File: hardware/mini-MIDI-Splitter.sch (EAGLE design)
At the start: 40 parts, among them IC1 6N138, IC2 4050D, IC3 REG1117, X1 DIN5PIN, X2 DIN5PIN, X3 DIN5PIN, X4 DIN5PIN, X5 DIN5PIN, X6 DIN5PIN

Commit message: updates
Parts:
- C3: device rcl:CPOL-EUE2-4 -> rcl:C-EUC0805
- C5: device rcl:C-EUC0805 -> rcl:CPOL-EUE2-4
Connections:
- net GND: now also C3.2, C5.-, R3.1; no longer C3.-, C5.2, R2.1
- net N$1: now also R5.2; no longer R4.2
- net N$11: now also R7.1; no longer R6.1
- net N$12: now also R5.1; no longer R4.1
- net N$14: now also R4.1; no longer R5.1
- net N$15: now also R6.1; no longer R7.1
- net N$16: now also R8.1; no longer R9.1
- net N$18: now also R12.1; no longer R18.1
- net N$19: now also R17.1; no longer R16.1
- net N$2: now also R7.2; no longer R6.2
- net N$20: now also R2.1; no longer R3.1
- net N$21: now also R2.2; no longer R3.2
- net N$22: now also R3.2; no longer R2.2
- net N$3: now also R9.2; no longer R8.2
- net N$5: now also R18.2; no longer R12.2
- net N$6: now also R16.2; no longer R17.2
- net N$7: now also R16.1; no longer R17.1
- net N$8: now also R9.1; no longer R8.1
- net N$9: now also R18.1; no longer R12.1
- net VCC: now also C1.1, C5.+, R12.2, R17.2, R4.2, R6.2, R8.2; no longer C4.+, C5.1, R16.2, R18.2, R5.2, R7.2, R9.2
- net VIN: now also C3.1, C4.+; no longer C1.1, C3.+
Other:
- moved on the sheet: C1, C4, R12, R16, R17, R18, R2, R3, R4, R5, R6, R7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

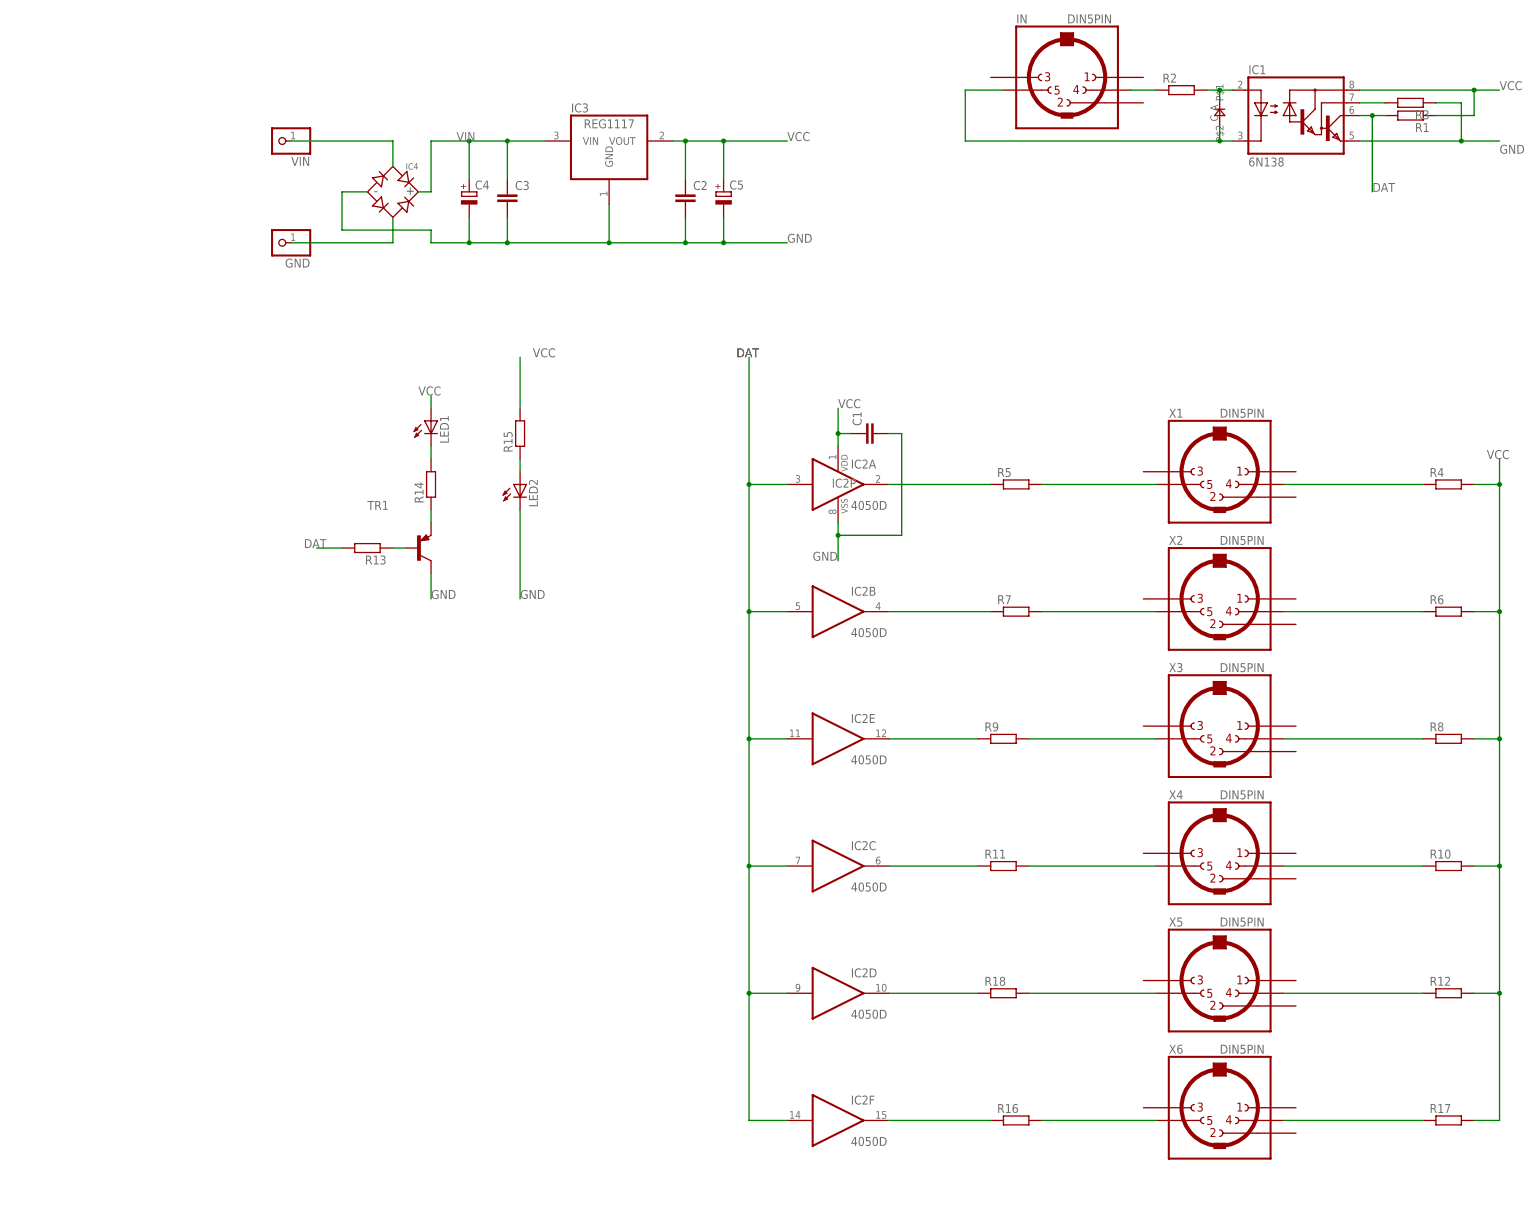
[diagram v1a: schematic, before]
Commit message: add component values
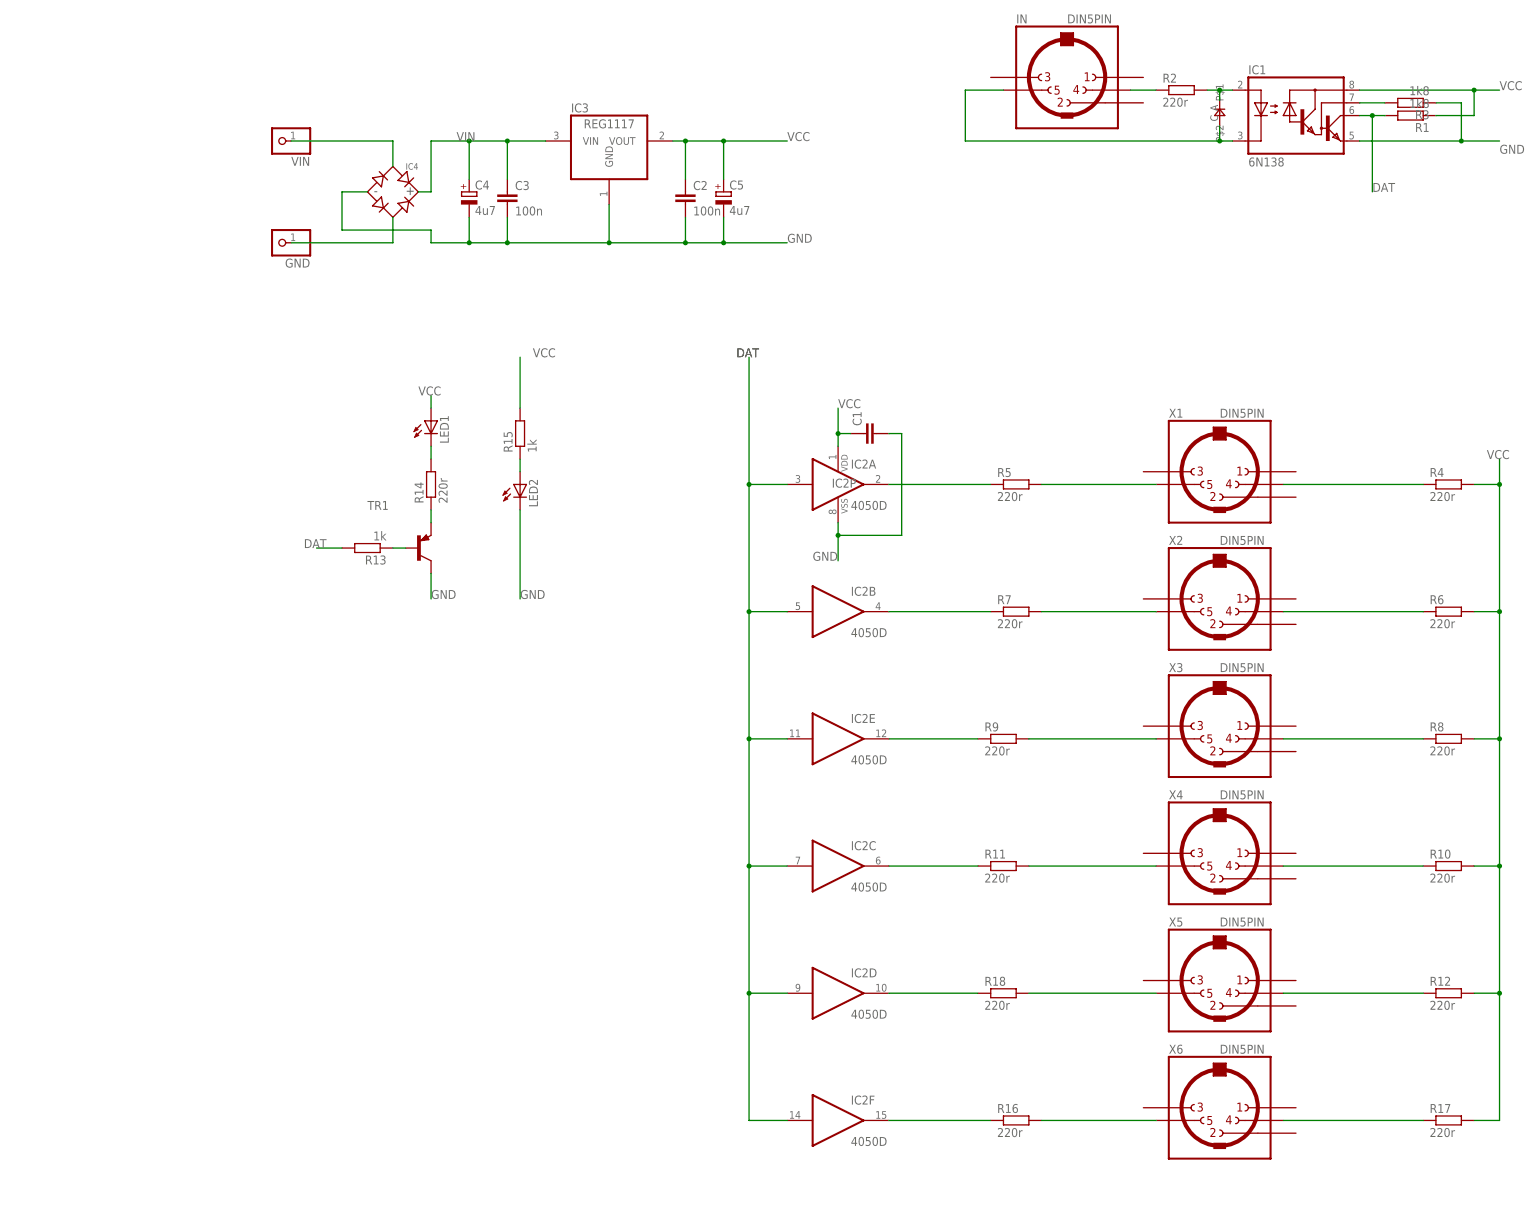
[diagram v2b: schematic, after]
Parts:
- C2, C3: value (none) -> 100n
- C4, C5: value (none) -> 4u7
- R1, R3: value (none) -> 1k8
- R10, R11, R12, R14, R16, R17, R18, R2, R4, R5, R6, R7, R8, R9: value (none) -> 220r
- R13, R15: value (none) -> 1k
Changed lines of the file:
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@@
 <part name="IN" library="jason_eagle6" deviceset="DIN5PIN" device=""/>
 <part name="IC2" library="40xx" deviceset="4050" device="D"/>
-<part name="R5" library="rcl" deviceset="R-EU_" device="R0805"/>
-<part name="R7" library="rcl" deviceset="R-EU_" device="R0805"/>
-<part name="R11" library="rcl" deviceset="R-EU_" device="R0805"/>
-<part name="R18" library="rcl" deviceset="R-EU_" device="R0805"/>
-<part name="R9" library="rcl" deviceset="R-EU_" device="R0805"/>
-<part name="R16" library="rcl" deviceset="R-EU_" device="R0805"/>
-<part name="R4" library="rcl" deviceset="R-EU_" device="R0805"/>
-<part name="R6" library="rcl" deviceset="R-EU_" device="R0805"/>
-<part name="R8" library="rcl" deviceset="R-EU_" device="R0805"/>
-<part name="R10" library="rcl" deviceset="R-EU_" device="R0805"/>
-<part name="R12" library="rcl" deviceset="R-EU_" device="R0805"/>
-<part name="R17" library="rcl" deviceset="R-EU_" device="R0805"/>
+<part name="R5" library="rcl" deviceset="R-EU_" device="R0805" value="220r"/>
+<part name="R7" library="rcl" deviceset="R-EU_" device="R0805" value="220r"/>
+<part name="R11" library="rcl" deviceset="R-EU_" device="R0805" value="220r"/>
+<part name="R18" library="rcl" deviceset="R-EU_" device="R0805" value="220r"/>
+<part name="R9" library="rcl" deviceset="R-EU_" device="R0805" value="220r"/>
+<part name="R16" library="rcl" deviceset="R-EU_" device="R0805" value="220r"/>
+<part name="R4" library="rcl" deviceset="R-EU_" device="R0805" value="220r"/>
+<part name="R6" library="rcl" deviceset="R-EU_" device="R0805" value="220r"/>
+<part name="R8" library="rcl" deviceset="R-EU_" device="R0805" value="220r"/>
+<part name="R10" library="rcl" deviceset="R-EU_" device="R0805" value="220r"/>
+<part name="R12" library="rcl" deviceset="R-EU_" device="R0805" value="220r"/>
+<part name="R17" library="rcl" deviceset="R-EU_" device="R0805" value="220r"/>
 <part name="IC1" library="optocoupler" deviceset="6N138" device=""/>
-<part name="R2" library="rcl" deviceset="R-EU_" device="R0805"/>
-<part name="R1" library="rcl" deviceset="R-EU_" device="R0805"/>
-<part name="R3" library="rcl" deviceset="R-EU_" device="R0805"/>
+<part name="R2" library="rcl" deviceset="R-EU_" device="R0805" value="220r"/>
+<part name="R1" library="rcl" deviceset="R-EU_" device="R0805" value="1k8"/>
+<part name="R3" library="rcl" deviceset="R-EU_" device="R0805" value="1k8"/>
 <part name="IC3" library="burr-brown" deviceset="REG1117" device=""/>
 <part name="VIN" library="pinhead" deviceset="PINHD-1X1" device=""/>
 <part name="GND" library="pinhead" deviceset="PINHD-1X1" device=""/>
 <part name="TR1" library="transistor" deviceset="*-PNP-" device="SOT23-BEC" technology="MMBT3906LT1"/>
-<part name="R14" library="rcl" deviceset="R-EU_" device="R0805"/>
-<part name="R13" library="rcl" deviceset="R-EU_" device="R0805"/>
+<part name="R14" library="rcl" deviceset="R-EU_" device="R0805" value="220r"/>
+<part name="R13" library="rcl" deviceset="R-EU_" device="R0805" value="1k"/>
 <part name="LED1" library="led" deviceset="LED" device="3MM"/>
 <part name="LED2" library="led" deviceset="LED" device="3MM"/>
-<part name="R15" library="rcl" deviceset="R-EU_" device="R0805"/>
-<part name="C3" library="rcl" deviceset="C-EU" device="C0805"/>
-<part name="C2" library="rcl" deviceset="C-EU" device="C0805"/>
-<part name="C4" library="rcl" deviceset="CPOL-EU" device="E2-4"/>
-<part name="C5" library="rcl" deviceset="CPOL-EU" device="E2-4"/>
+<part name="R15" library="rcl" deviceset="R-EU_" device="R0805" value="1k"/>
+<part name="C3" library="rcl" deviceset="C-EU" device="C0805" value="100n"/>
+<part name="C2" library="rcl" deviceset="C-EU" device="C0805" value="100n"/>
+<part name="C4" library="rcl" deviceset="CPOL-EU" device="E2-4" value="4u7"/>
+<part name="C5" library="rcl" deviceset="CPOL-EU" device="E2-4" value="4u7"/>
 <part name="D1" library="jasons_stuff" deviceset="0805DIODE" device=""/>
 <part name="IC4" library="microbuilder" deviceset="BRIDGERECTIFIER" device=""/>

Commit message: REV3 PCB
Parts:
- removed GND, VIN: (no value), pinhead:PINHD-1X1
- removed LED2: (no value), led:LED3MM
- removed TR1: (no value), transistor:MMBT3906LT1-PNP-SOT23-BEC
- added C6: 4u7, rcl:CPOL-EUE2-4
- added CLK, PWR: (no value), led:LED3MM
- added IC5: (no value), microbuilder:BRIDGERECTIFIER
- added ICSP: (no value), tag-connect:TC2030-MCP-NL
- added RA2, RA4: (no value), pinhead:PINHD-1X1
- added U$1: PWR_SOCKET_2_1MM, jason_eagle6:PWR_SOCKET_2_1MM
- added X7: VERTICAL_3_5MM_SOCKET, jason_eagle6:VERTICAL_3_5MM_SOCKET
- C1: value (none) -> 100n
- C3: value 100n -> (none)
- C4: value 4u7 -> 100n; device rcl:CPOL-EUE2-4 -> rcl:C-EUC0805
- IC1: value 6N138 -> REG1117; device optocoupler:6N138 -> burr-brown:REG1117
- IC3: value REG1117 -> PIC12F1822SO08; device burr-brown:REG1117 -> jasons_stuff:PIC12F1822SO08
- IC4: value (none) -> 6N138; device microbuilder:BRIDGERECTIFIER -> optocoupler:6N138
- R1: value 1k8 -> 1k
- R13, R15: value 1k -> 220r
- R17, R18: value 220r -> 1k8
- R3: value 1k8 -> 220r
- renumbered LED1 to DAT
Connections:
- removed net DAT: IC1.VO, IC2A.I, IC2B.I, IC2C.I, IC2D.I, IC2E.I, IC2F.I, R1.2, R13.2
- removed net N$26: LED2.A, R15.1
- new net CLK: CLK.C, R2.2
- new net CLK_LED: CLK.A, IC3.RA1/PGC, ICSP.ICSP_CLK/PGC
- new net DAT_LED: DAT.A, IC3.RA0/PGD, ICSP.ICSP_DAT/PGD
- new net MIDI_IN: IC2A.I, IC2B.I, IC2C.I, IC2D.I, IC2E.I, IC2F.I, IC3.RA5, IC4.VO, R18.2
- new net MIDI_OUT: IC3.RA4, RA4.1
- new net N$33: IC3.MCLR#/VPP/RA3, ICSP.VPP/MCLR
- net GND: now also C4.2, C6.-, IC3.VSS, IC4.GND, IC5.-, ICSP.VSS(GND), R1.1, R17.1, R2.1; no longer C4.-, IC3.GND, IC4.-, LED2.C, TR1.C
- net N$1: now also R14.2; no longer R5.2
- net N$10: now also R8.1; no longer R11.1
- net N$11: now also IC2A.O, R4.1; no longer IC2B.O, R7.1
- net N$12: now also IC2B.O, R6.1; no longer IC2A.O, R5.1
- net N$13: now also PWR.C, R1.2; no longer R14.1, TR1.E
- net N$14: now also R15.1; no longer R4.1
- net N$15: now also R13.1; no longer R6.1
- net N$16: now also R11.1; no longer R8.1
- net N$17: now also R9.1; no longer R10.1
- net N$18: now also R7.1; no longer R12.1
- net N$19: now also R5.1; no longer R17.1
- net N$2: now also R12.2; no longer R7.2
- net N$20: now also R16.1, X7.4; no longer R2.1
- net N$21: now also IC4.A, R16.2; no longer IC1.A, R2.2
- net N$22: now also IC4.VB, R17.2; no longer IC1.VB, R3.2
- net N$23: now also R3.2; no longer R14.2
- net N$24: now also IC4.C, X7.3; no longer IC1.C
- net N$25: now also IC3.RA2, RA2.1; no longer R13.1, TR1.B
- net N$27: now also IC5.AC1, U$1.BARREL; no longer IC4.AC1, VIN.1
- net N$28: now also IC5.AC2, U$1.PIN; no longer GND.1, IC4.AC2
- net N$3: now also R10.2; no longer R9.2
- net N$4: now also R8.2; no longer R11.2
- net N$5: now also R6.2; no longer R18.2
- net N$6: now also R4.2; no longer R16.2
- net N$7: now also R14.1; no longer R16.1
- net N$8: now also R12.1; no longer R9.1
- net N$9: now also R10.1; no longer R18.1
- net VCC: now also C3.1, C4.1, IC1.VOUT, IC3.VDD, IC4.VCC, ICSP.VDD, PWR.A, R11.2, R13.2, R18.1, R5.2, R7.2, R9.2; no longer C1.1, DAT.A, IC1.VCC, IC3.VOUT, R1.1, R10.2, R12.2, R17.2, R4.2, R6.2, R8.2
- net VIN: now also C1.1, C6.+, IC1.VIN, IC5.+; no longer C3.1, C4.+, IC3.VIN, IC4.+
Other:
- note added: "BANANA SPLIT REV3"
- note added: "Jason Hotchkiss"
- note added: "MIDI INPUT"
- note added: "MIDI OUTPUTS"
- note added: "POWER SUPPLY"
- note added: "PROCESSOR"
- moved on the sheet: C1, C2, C3, C5, IC2A, IC2B, IC2C, IC2D, IC2E, IC2F, IN, R1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
